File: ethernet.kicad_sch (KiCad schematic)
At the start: 32 parts, among them J5 1888250-3, U3 W5500, X1 25MHz

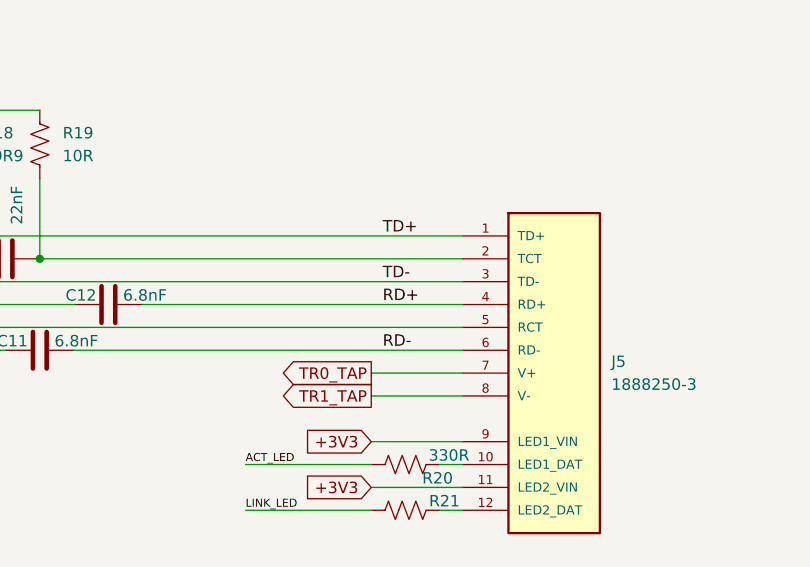
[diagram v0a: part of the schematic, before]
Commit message: Cleanup and added PoE header
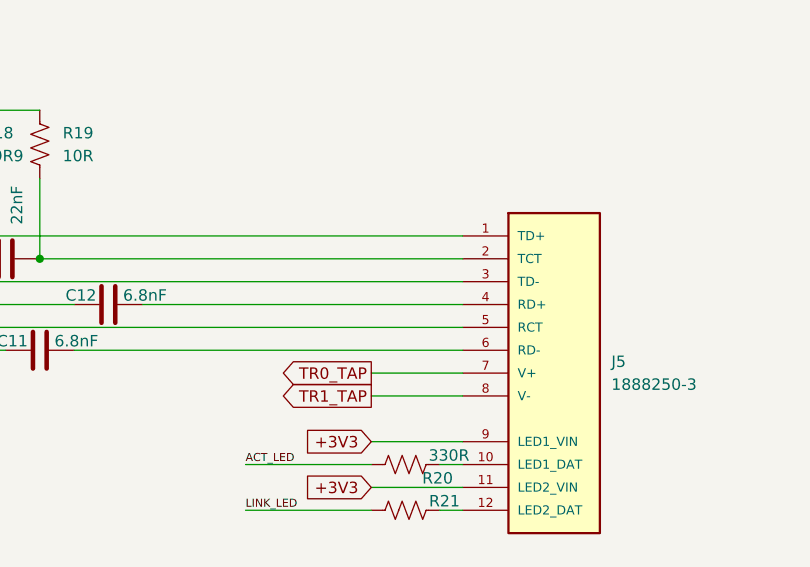
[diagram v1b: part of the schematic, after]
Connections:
- net RD+: no longer names the net of C12.1, J5.4 (RD+)
- net RD-: no longer names the net of C11.1, J5.6 (RD-)
- net TD+ renamed TX+
- net TD- renamed TX-
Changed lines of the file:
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@@
-		)
-	)
-	(label "RD-"
-		(at 177.8 57.15 0)
-		(fields_autoplaced yes)
-		(effects
-			(font
-				(size 1.27 1.27)
-			)
-			(justify left bottom)
 		)
 	)
@@
 			)
 			(justify left bottom)
-		)
-	)
-	(label "RD+"
-		(at 177.8 52.07 0)
-		(fields_autoplaced yes)
-		(effects
-			(font
-				(size 1.27 1.27)
-			)
-			(justify left bottom)
-		)
-	)
-	(label "TD+"
-		(at 177.8 44.45 0)
-		(fields_autoplaced yes)
-		(effects
-			(font
-				(size 1.27 1.27)
-			)
-			(justify left bottom)
-		)
-	)
-	(label "TD-"
-		(at 177.8 49.53 0)
-		(fields_autoplaced yes)
-		(effects
-			(font
-				(size 1.27 1.27)
-			)
-			(justify left bottom)

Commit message: Recent updates
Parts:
- removed X1: 25MHz, Crystal:Crystal_SMD_TXC_9HT11-2Pin_2.0x1.2mm_HandSoldering, symbol seeed-eagle-import:CRYSTAL'5032'
- added Y1: 830081609, CrystalOscillator:830081609, symbol CrystalOscillator:830081609
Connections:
- net at R12.2, U3.30 (XI/CLKIN): now also Y1.3 (CRYSTAL_2); no longer C5.1
- net at R12.1, U3.31 (XO): now also Y1.1 (CRYSTAL_1); no longer C6.1
- net TR0_TAP renamed V+
- net TR1_TAP renamed V-
- new net: C5.1, Y1.2 (GND_1)
- new net: C6.1, Y1.4 (GND_2)
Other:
- moved on the sheet: C5, C6, R12
